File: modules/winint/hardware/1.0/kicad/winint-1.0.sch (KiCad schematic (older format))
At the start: 66 parts, among them J1 ROT, J2 Screw_Terminal_01x03, J3 Screw_Terminal_01x03, J4 Screw_Terminal_01x05, J5 DOK, J6 STP, J7 DEP, J8 RET, J9 OVL, K1 RS_476-257, K2 RS_476-257, Q1 NTE123A, Q2 NTE123A, SW1 INSTANCE, U1 ROT, U2 DOK, U3 STP, U4 DEP, U5 RET, U6 OVL, U7 Teensy_3.2, U8 MCP2551-I-P, U9 TEC2-2411WI

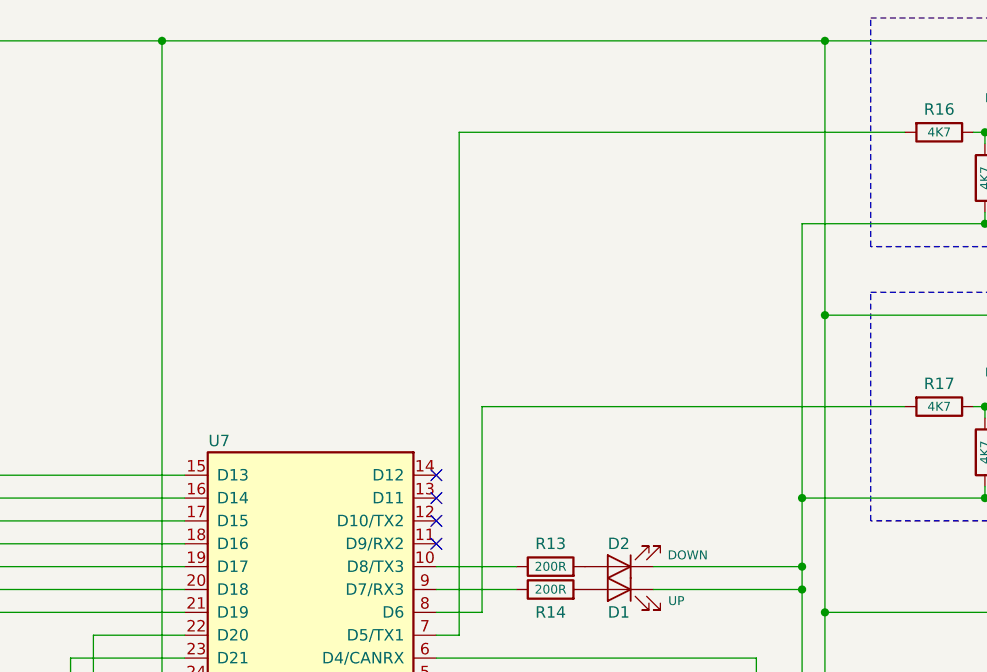
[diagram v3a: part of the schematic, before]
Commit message: Added relay disable jumper
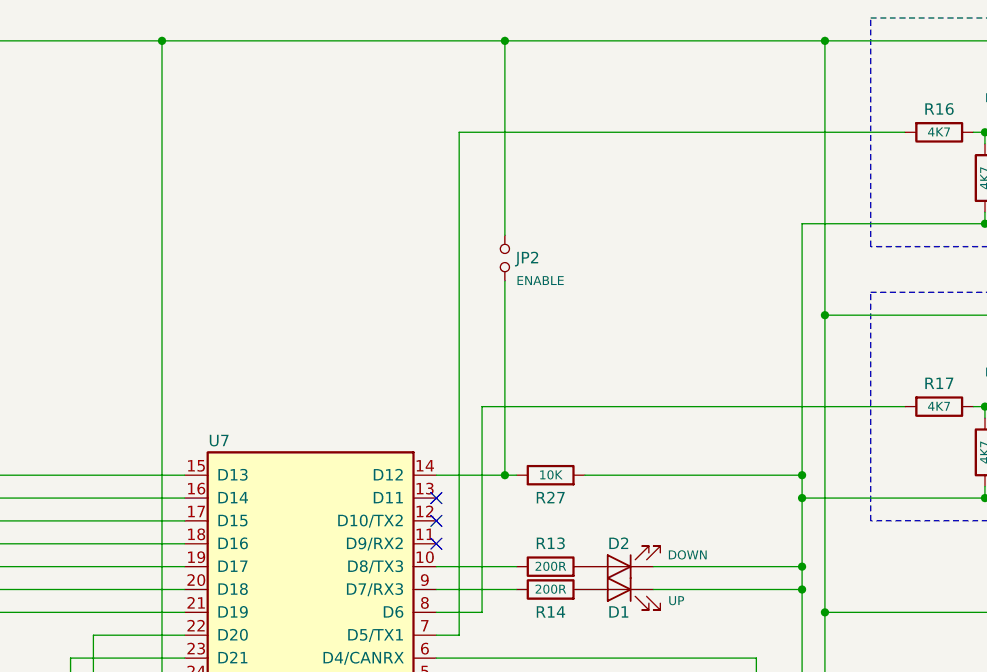
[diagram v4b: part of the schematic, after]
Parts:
- added JP2: ENABLE, Connector_PinHeader_2.54mm:PinHeader_1x02_P2.54mm_Vertical, symbol Device:Jumper_NO_Small
- added R27: 10K, Resistor_THT:R_Axial_DIN0204_L3.6mm_D1.6mm_P5.08mm_Horizontal, symbol Device:R
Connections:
- net 5VDC: now also JP2.2
- net GND: now also R27.2
- net at U7.14 (D12): now also JP2.1, R27.1
- no-connect marks 7 -> 6
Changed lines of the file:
@@
 	1    0    0    -1
 $EndComp
-NoConn ~ 4900 2700
 NoConn ~ 4900 2800
 NoConn ~ 4900 2900
@@
 	6500 5450 7550 5450
 Wire Wire Line
-	6500 2800 6500 1600
+	6500 2800 6500 2700
 Wire Wire Line
 	6500 1600 7300 1600
@@
 	5100 2400 5100 3300
 Wire Wire Line
-	3700 800  6600 800
+	3700 800  5200 800
 Text Label 10000 1800 2    50   Italic 0
 RELAY
@@
 Wire Wire Line
 	7950 2450 7950 2350
+$Comp
+L Device:Jumper_NO_Small JP2
+U 1 1 5FC163D4
+P 5200 1750
+F 0 "JP2" V 5200 1650 50  0000 C CNN
+F 1 "ENABLE" V 5100 1700 39  0000 R CNN
+F 2 "Connector_PinHeader_2.54mm:PinHeader_1x02_P2.54mm_Vertical" H 5200 1750 50  0001 C CNN
+F 3 "~" H 5200 1750 50  0001 C CNN
+	1    5200 1750
+	0    -1   -1   0
+$EndComp
+$Comp
+L Device:R R27
+U 1 1 5FC1A576
+P 5400 2700
+F 0 "R27" V 5300 2700 50  0000 C CNN
+F 1 "10K" V 5400 2700 39  0000 C CNN
+F 2 "Resistor_THT:R_Axial_DIN0204_L3.6mm_D1.6mm_P5.08mm_Horizontal" V 5330 2700 50  0001 C CNN
+F 3 "~" H 5400 2700 50  0001 C CNN
+F 4 "1W" V 5400 2700 50  0001 C CNN "Power"
+	1    5400 2700
+	0    -1   -1   0
+$EndComp
+Wire Wire Line
+	5250 2700 5200 2700
+Connection ~ 6500 2700
+Wire Wire Line
+	6500 2700 6500 1600
+Wire Wire Line
+	5550 2700 6500 2700
+Wire Wire Line
+	5200 2700 5200 1850
+Connection ~ 5200 2700
+Wire Wire Line
+	5200 2700 4900 2700
+Wire Wire Line
+	5200 1650 5200 800
+Connection ~ 5200 800
+Wire Wire Line
+	5200 800  6600 800
 $EndSCHEMATC

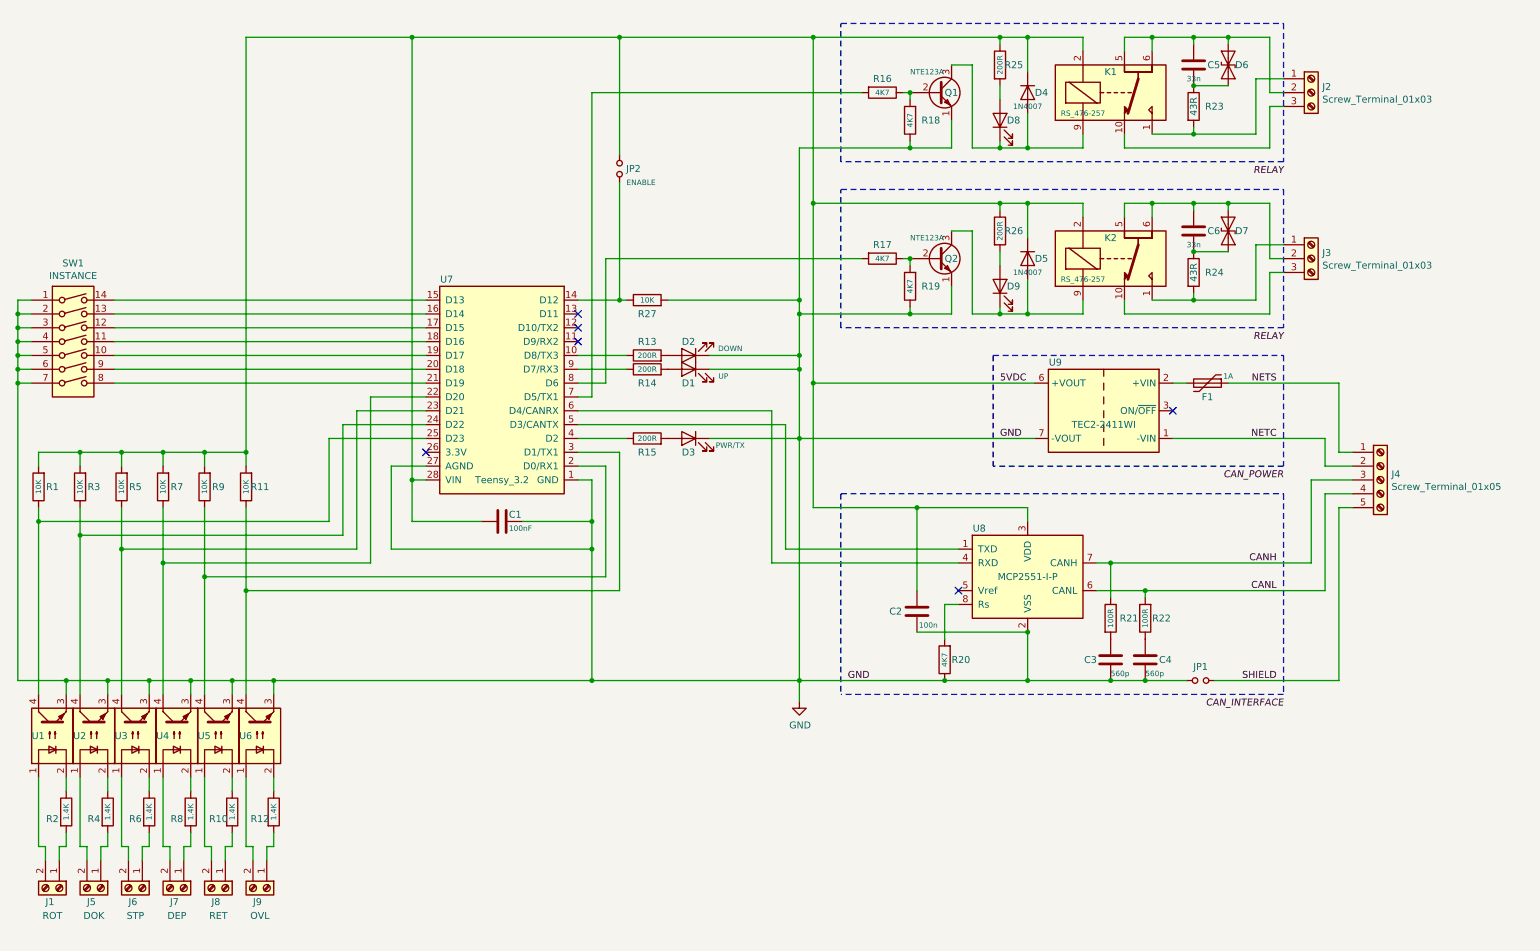
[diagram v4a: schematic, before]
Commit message: Modified CONFIG switch operation
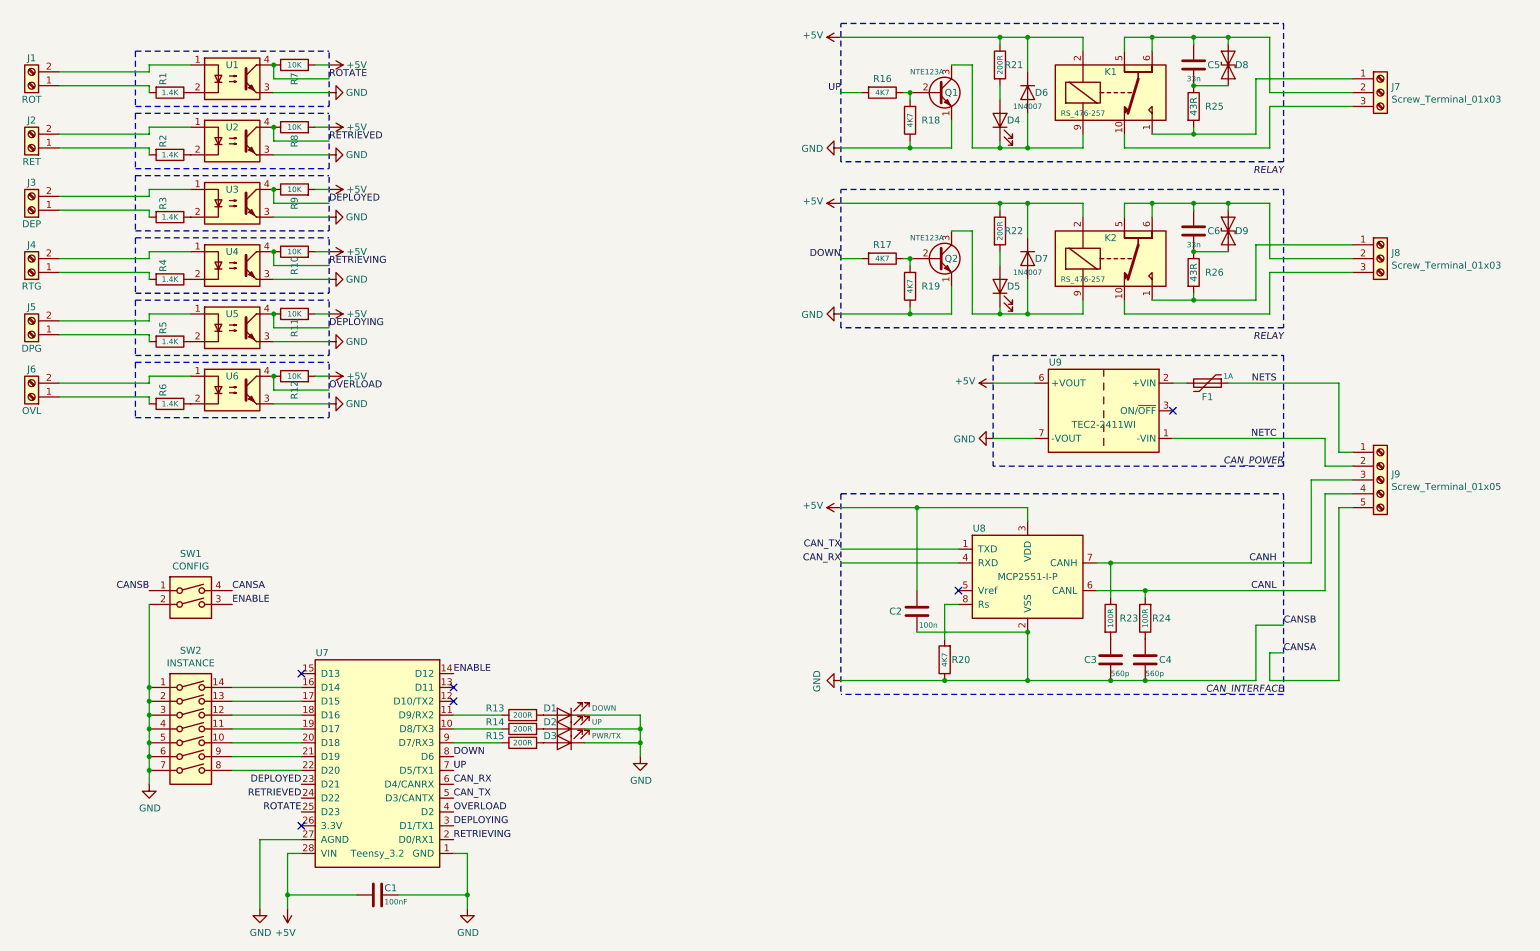
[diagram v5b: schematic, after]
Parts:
- removed J7: DEP, TerminalBlock_Phoenix:TerminalBlock_Phoenix_MPT-0,5-2-2.54_1x02_P2.54mm_Horizontal, symbol Connector:Screw_Terminal_01x02
- removed J8: RET, TerminalBlock_Phoenix:TerminalBlock_Phoenix_MPT-0,5-2-2.54_1x02_P2.54mm_Horizontal, symbol Connector:Screw_Terminal_01x02
- removed J9: OVL, TerminalBlock_Phoenix:TerminalBlock_Phoenix_MPT-0,5-2-2.54_1x02_P2.54mm_Horizontal, symbol Connector:Screw_Terminal_01x02
- removed JP1: SCR, Connector_PinHeader_2.54mm:PinHeader_1x02_P2.54mm_Vertical, symbol Device:Jumper_NO_Small
- removed JP2: ENABLE, Connector_PinHeader_2.54mm:PinHeader_1x02_P2.54mm_Vertical, symbol Device:Jumper_NO_Small
- removed R27, R7: 10K, Resistor_THT:R_Axial_DIN0204_L3.6mm_D1.6mm_P5.08mm_Horizontal, symbol Device:R
- added J2: RET, TerminalBlock_Phoenix:TerminalBlock_Phoenix_MPT-0,5-2-2.54_1x02_P2.54mm_Horizontal, symbol Connector:Screw_Terminal_01x02
- added J3: DEP, TerminalBlock_Phoenix:TerminalBlock_Phoenix_MPT-0,5-2-2.54_1x02_P2.54mm_Horizontal, symbol Connector:Screw_Terminal_01x02
- added J4: RTG, TerminalBlock_Phoenix:TerminalBlock_Phoenix_MPT-0,5-2-2.54_1x02_P2.54mm_Horizontal, symbol Connector:Screw_Terminal_01x02
- added R2: 1.4K, Resistor_THT:R_Axial_DIN0204_L3.6mm_D1.6mm_P5.08mm_Horizontal, symbol Device:R
- added SW1: CONFIG, Button_Switch_THT:SW_DIP_SPSTx02_Slide_6.7x6.64mm_W7.62mm_P2.54mm_LowProfile, symbol Switch:SW_DIP_x02
- J5: value DOK -> DPG
- J6: value STP -> OVL
- R10, R12, R8: value 1.4K -> 10K
- R3, R5: value 10K -> 1.4K
- SW2: renamed from SW1; footprint Package_DIP:DIP-14_W7.62mm -> Button_Switch_THT:SW_DIP_SPSTx07_Slide_6.7x19.34mm_W7.62mm_P2.54mm_LowProfile
- U1: value ROT -> PC817
- U2: value DOK -> PC817
- U3: value STP -> PC817
- U4: value DEP -> PC817
- U5: value RET -> PC817
- U6: value OVL -> PC817
- renumbered D2 to D1, D1 to D2, D8 to D4, D9 to D5, D4 to D6, D5 to D7, D6 to D8, D7 to D9, J2 to J7, J3 to J8, J4 to J9, R2 to R1, R25 to R21, R26 to R22, R21 to R23, R22 to R24, R23 to R25, R24 to R26, R1 to R7
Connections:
- net GND: now also SW1.1, SW1.2
- net CAN_TX: now reaches U7.5 (D3/CANTX), U8.1 (TXD)
- net CAN_RX: now reaches U7.6 (D4/CANRX), U8.4 (RXD)
- net at R15.1: now also U7.9 (D7/RX3); no longer U7.4 (D2)
- net at U7.10 (D8/TX3): now also R14.1; no longer R13.1
- net at U7.11 (D9/RX2): now also R13.1
- net ENABLE: now reaches U7.14 (D12)
- net ENABLE: now also SW1.3
- net at U7.15 (D13): no longer SW2.14
- net at U7.16 (D14): now also SW2.14; no longer SW2.13
- net at U7.17 (D15): now also SW2.13; no longer SW2.12
- net at U7.18 (D16): now also SW2.12; no longer SW2.11
- net at U7.19 (D17): now also SW2.11; no longer SW2.10
- net at U7.20 (D18): now also SW2.10; no longer SW2.9
- net at U7.21 (D19): now also SW2.9; no longer SW2.8
- net at U7.22 (D20): now also SW2.8; no longer U4.4
- net DEPLOYED: now reaches U3.4, U7.23 (D21)
- net DEPLOYED: now also R9.1; no longer R5.1
- net RETRIEVED: now reaches U2.4, U7.24 (D22)
- net RETRIEVED: now also R8.1; no longer R3.1
- net ROTATE: now reaches R7.1, U1.4, U7.25 (D23)
- net DEPLOYING: now reaches R11.1, U7.3 (D1/TX1)
- net DEPLOYING: now also U5.4; no longer U6.4
- net UP: now reaches R16.2, U7.7 (D5/TX1)
- net DOWN: now reaches R17.2, U7.8 (D6)
- net at U2.1: now also J2.2 (Pin_2); no longer J5.2 (Pin_2)
- net at U2.2: now also R2.1; no longer R4.1
- net at U3.1: now also J3.2 (Pin_2); no longer J6.2 (Pin_2)
- net at U3.2: now also R3.1; no longer R6.1
- net at U4.1: now also J4.2 (Pin_2)
- net at U4.2: now also R4.1; no longer R8.1
- net at U5.1: now also J5.2 (Pin_2)
- net at U5.2: now also R5.1; no longer R10.1
- net at U6.1: now also J6.2 (Pin_2)
- net at U6.2: now also R6.1; no longer R12.1
- net at R4.2: now also J4.1 (Pin_1); no longer J5.1 (Pin_1)
- net +5V: now reaches R8.2
- net +5V: now also C1.1, C2.1, D6.1 (K), D7.1 (K), K1.2, K2.2, R10.2, R11.2, R12.2, R21.1, R22.1, R7.2, R9.2, U7.28 (VIN), U8.3 (VDD), U9.6 (+VOUT)
- removed net 5VDC: C1.1, C2.1, D6.1 (K), D7.1 (K), K1.2, K2.2, R11.2, R21.1, R22.1, R3.2, R5.2, R7.2, R9.2, U7.28 (VIN), U8.3 (VDD), U9.6 (+VOUT)
- net SHIELD renamed CANSA
- net CANSA: now also SW1.4
- new net: J2.1 (Pin_1), R2.2
- new net: J3.1 (Pin_1), R3.2
- new net: J5.1 (Pin_1), R5.2
- new net OVERLOAD: R12.1, U6.4, U7.4 (D2)
- new net RETRIEVING: R10.1, U4.4, U7.2 (D0/RX1)
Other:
- moved on the sheet: C1, D1, D2, D3, J1, J7, J8, R1, R13, R14, R15, R7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

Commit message: Tidy up
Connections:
- net LED_PWR: now reaches R15.1, U7.9 (D7/RX3)
- net LED_UP: now reaches R14.1, U7.10 (D8/TX3)
- net LED_DN: now reaches R13.1, U7.11 (D9/RX2)
- net UP_CO: now reaches C5.2, D8.1 (A1), J7.2 (Pin_2), K1.5, K1.6
- net UP-NO: now reaches J7.1 (Pin_1), K1.1, R25.2
- net UP_NC: now reaches J7.3 (Pin_3), K1.10
- net DN-NO: now reaches J8.1 (Pin_1), K2.1, R26.2
- net DN_CO: now reaches C6.2, D9.1 (A1), J8.2 (Pin_2), K2.5, K2.6
- net DN_NC: now reaches J8.3 (Pin_3), K2.10
- net CANSA renamed CANSCR
- net DEPLOYED renamed SENSOR_DPD
- net DEPLOYING renamed SENSOR_DPG
- net DOWN renamed RELAY_DOWN
- net OVERLOAD renamed SENSOR_OVL
- net RETRIEVED renamed SENSOR_RTD
- net RETRIEVING renamed SENSOR_RTG
- net ROTATE renamed SENSOR_ROT
- net UP renamed RELAY_UP
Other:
- note added: "12/5 V DC-DC CONVERTER"
- note added: "CAN INTERFACE"
- note added: "OUTPUT RELAY (DOWN)"
- note added: "OUTPUT RELAY (UP)"
- note added: "SENSOR INPUTS - ALL SIGNALS ACTIVE LOW"
- moved on the sheet: C1, C2, C3, C4, C6, D1, D2, D3, D5, D7, D9, F1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

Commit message: README update
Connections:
- net CANH renamed CAN_H
- net CANL renamed CAN_L
- net CANSCR renamed CAN_SCR
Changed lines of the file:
@@
 Connection ~ 7350 3900
 Text Label 10000 4300 2    50   ~ 0
-CANH
+CAN_H
 Text Label 10000 4500 2    50   ~ 0
-CANL
+CAN_L
 Wire Notes Line
 	6800 3800 10000 3800
@@
 $EndComp
 Text Label 2900 4350 0    50   ~ 0
-CANSCR
+CAN_SCR
 Wire Wire Line
 	8650 5500 9150 5500
@@
 RELAY_DOWN
 Text Label 10000 4950 2    50   ~ 0
-CANSCR
+CAN_SCR
 Wire Wire Line
 	2300 4450 2300 4350

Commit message: Tidy
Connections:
- net NETC renamed NET_C
- net NETS renamed NET_S
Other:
- moved on the sheet: J9
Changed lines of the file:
@@
 Wire Wire Line
 	9200 3100 9300 3100
-Text Label 10000 3100 2    50   ~ 0
-NETS
-Text Label 10000 3500 2    50   ~ 0
-NETC
+Text Label 10000 3100 0    50   ~ 0
+NET_S
+Text Label 10000 3500 0    50   ~ 0
+NET_C
 Wire Notes Line
 	7900 2900 10000 2900
@@
 Wire Notes Line
 	7900 2900 7900 3700
-$Comp
-L Connector:Screw_Terminal_01x05 J9
-U 1 1 6069075F
-P 10700 3300
-F 0 "J9" H 10780 3342 50  0000 L CNN
-F 1 "Screw_Terminal_01x05" H 10780 3251 50  0000 L CNN
-F 2 "TerminalBlock_Phoenix:TerminalBlock_Phoenix_MPT-0,5-5-2.54_1x05_P2.54mm_Horizontal" H 10700 3300 50  0001 C CNN
-F 3 "~" H 10700 3300 50  0001 C CNN
-	1    10700 3300
-	1    0    0    -1
-$EndComp
 Wire Wire Line
 	6800 4300 7650 4300
@@
 P 6800 5150
 F 0 "#PWR023" H 6800 4900 50  0001 C CNN
-F 1 "GND" H 6805 4977 50  0000 C CNN
+F 1 "GND" V 6800 4950 50  0000 C CNN
 F 2 "" H 6800 5150 50  0001 C CNN
 F 3 "" H 6800 5150 50  0001 C CNN
@@
 Wire Notes Line
 	800  3650 3100 3650
-Wire Wire Line
-	10400 3500 10500 3500
-Wire Wire Line
-	10400 3500 10400 5150
-Wire Wire Line
-	9600 3100 10500 3100
-Wire Wire Line
-	10300 3400 10500 3400
-Wire Wire Line
-	10300 3400 10300 4500
-Wire Wire Line
-	10200 3300 10500 3300
-Wire Wire Line
-	10200 3300 10200 4300
-Wire Wire Line
-	10100 3200 10500 3200
-Wire Wire Line
-	9200 3500 10100 3500
-Wire Wire Line
-	10100 3200 10100 3500
 Connection ~ 8750 4300
 Wire Wire Line
@@
 P 10000 5500
 F 0 "#PWR0101" H 10000 5250 50  0001 C CNN
-F 1 "GND" V 10005 5327 50  0000 C CNN
+F 1 "GND" V 10000 5300 50  0000 C CNN
 F 2 "" H 10000 5500 50  0001 C CNN
 F 3 "" H 10000 5500 50  0001 C CNN
@@
 P 10000 5900
 F 0 "#PWR0102" H 10000 5650 50  0001 C CNN
-F 1 "GND" V 10005 5727 50  0000 C CNN
+F 1 "GND" V 10000 5700 50  0000 C CNN
 F 2 "" H 10000 5900 50  0001 C CNN
 F 3 "" H 10000 5900 50  0001 C CNN
@@
 P 10000 6300
 F 0 "#PWR0103" H 10000 6050 50  0001 C CNN
-F 1 "GND" V 10005 6127 50  0000 C CNN
+F 1 "GND" V 10000 6100 50  0000 C CNN
 F 2 "" H 10000 6300 50  0001 C CNN
 F 3 "" H 10000 6300 50  0001 C CNN
@@
 	2300 4450 2300 4350
 Connection ~ 2300 4450
+Wire Wire Line
+	10400 3100 10400 3400
+Wire Wire Line
+	10400 3400 10500 3400
+Wire Wire Line
+	9600 3100 10400 3100
+Wire Wire Line
+	10500 3800 10400 3800
+Wire Wire Line
+	10400 3800 10400 5150
+$Comp
+L Connector:Screw_Terminal_01x05 J9
+U 1 1 6069075F
+P 10700 3600
+F 0 "J9" H 10780 3642 50  0000 L CNN
+F 1 "Screw_Terminal_01x05" H 10780 3551 50  0000 L CNN
+F 2 "TerminalBlock_Phoenix:TerminalBlock_Phoenix_MPT-0,5-5-2.54_1x05_P2.54mm_Horizontal" H 10700 3600 50  0001 C CNN
+F 3 "~" H 10700 3600 50  0001 C CNN
+	1    10700 3600
+	1    0    0    -1
+$EndComp
+Wire Wire Line
+	10500 3700 10300 3700
+Wire Wire Line
+	10300 3700 10300 4500
+Wire Wire Line
+	10500 3600 10200 3600
+Wire Wire Line
+	10200 3600 10200 4300
+Wire Wire Line
+	9200 3500 10500 3500
 $EndSCHEMATC
